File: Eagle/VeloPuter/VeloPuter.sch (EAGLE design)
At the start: 38 parts, among them IC1 LM2931, IC2 B7546, IC3 B7546

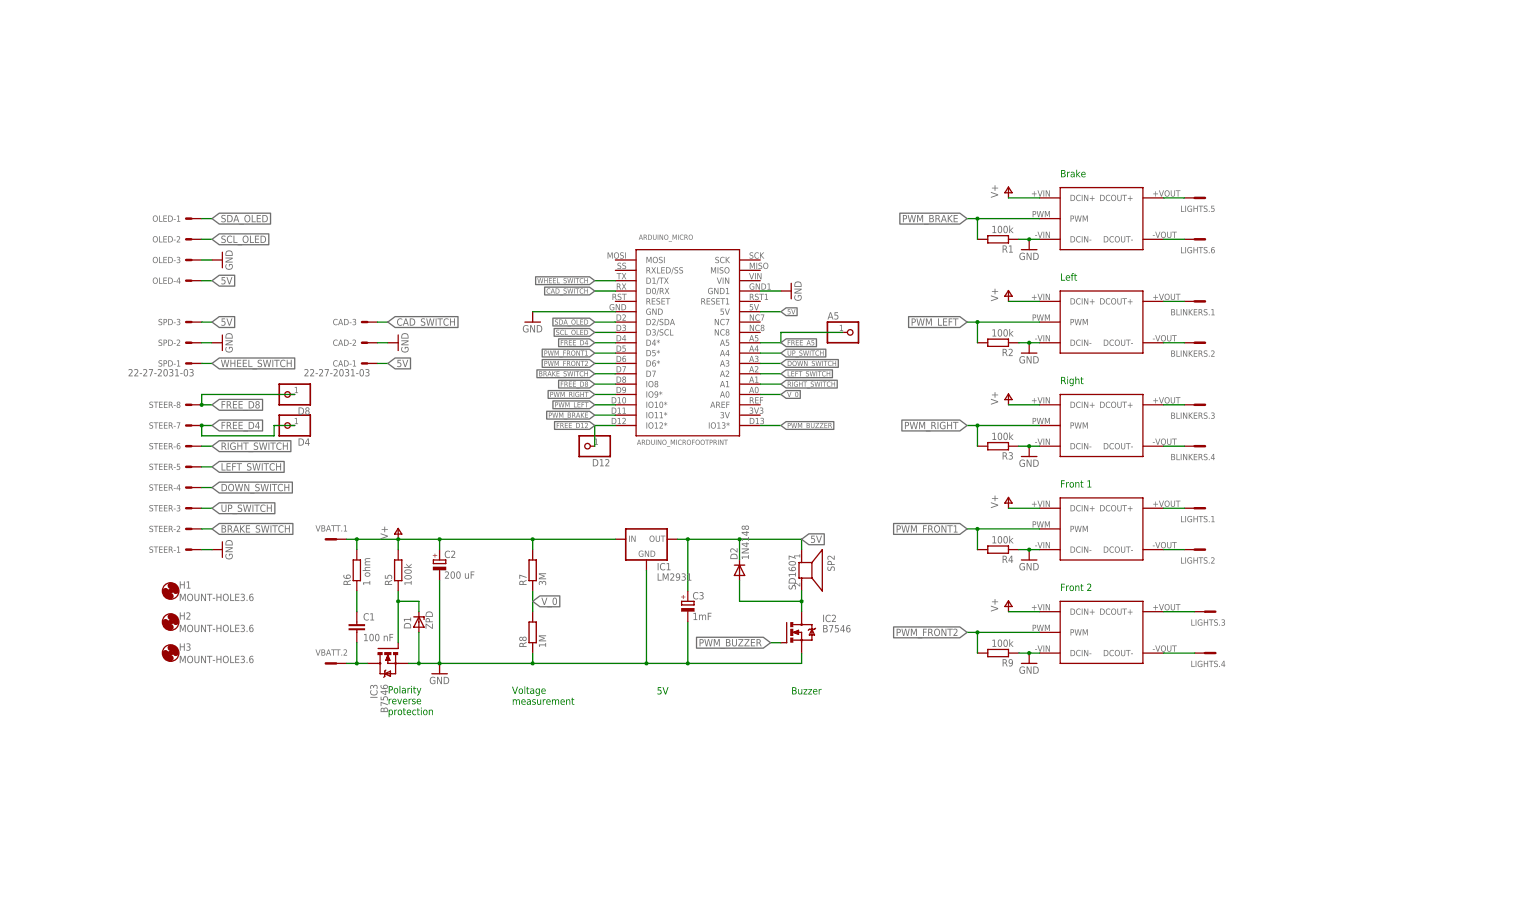
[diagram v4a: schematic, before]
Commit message: Started working on the PCB again. Adding swtichoff of the ALL Ldd's. Also: adding a 6th LDDd.
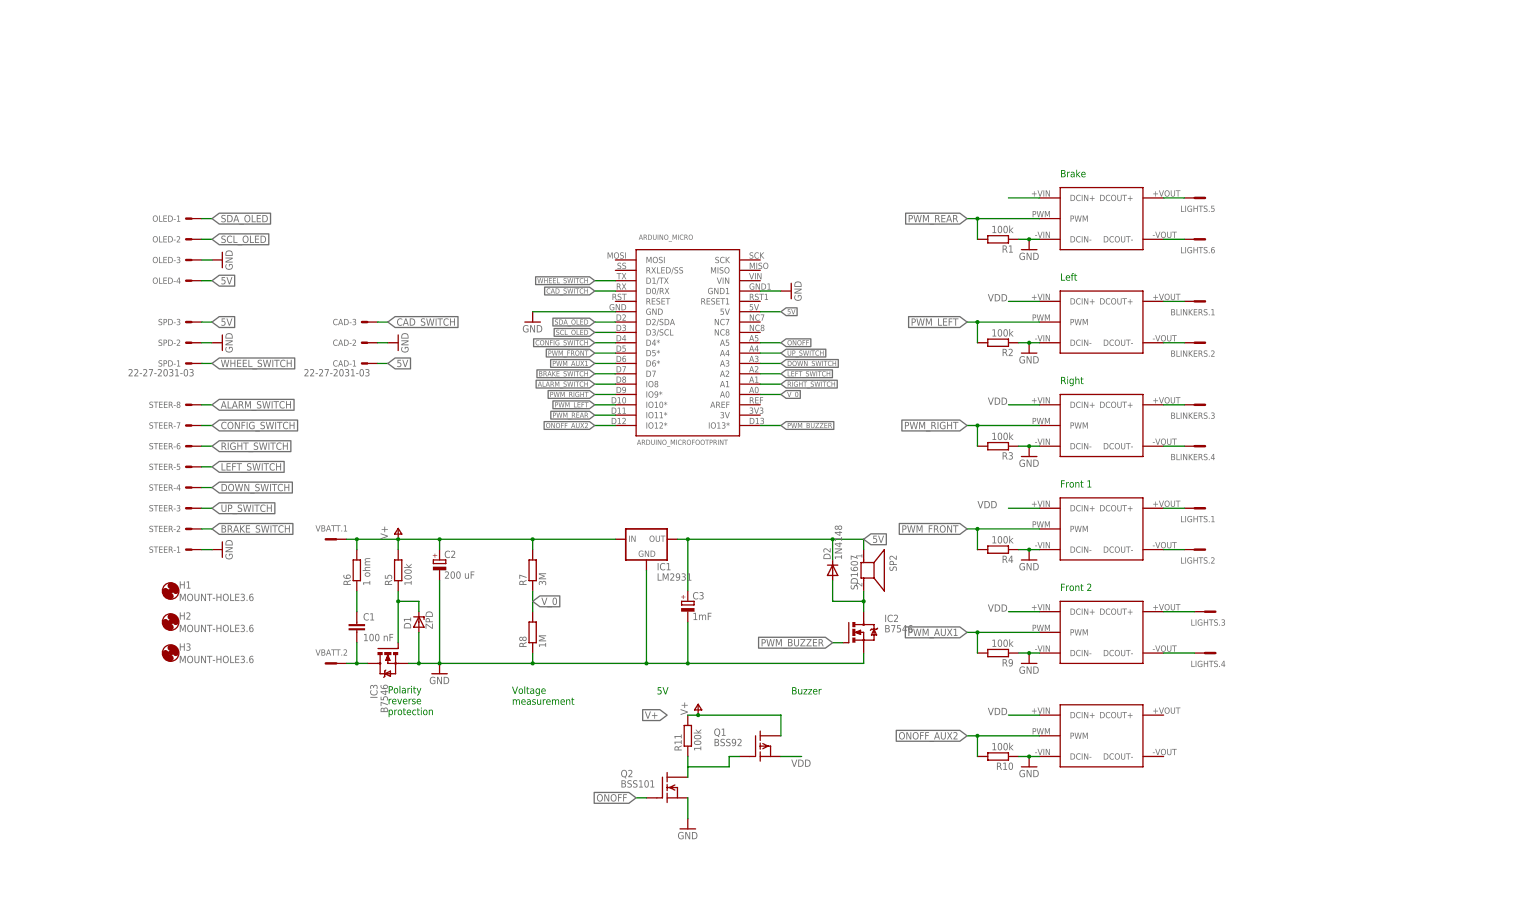
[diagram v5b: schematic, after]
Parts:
- removed A5, D12, D4, D8: (no value), pinhead:PINHD-1X1
- added Q1: BSS92, transistor-fet:BSS92
- added Q2: BSS101, transistor-fet:BSS101
- added R10, R11: 100k, resistor:R-EU_0207/10
- added U$1: LDD-L, meanwell_dcdc:LDD-L
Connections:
- net PWM_BRAKE renamed PWM_REAR
- net PWM_FRONT1 renamed PWM_FRONT
- net PWM_FRONT2 renamed PWM_AUX1
- removed net FREE_A5: A5.1, ARDUINO_MICRO.A5
- removed net FREE_D12: ARDUINO_MICRO.IO12*, D12.1
- removed net FREE_D4: ARDUINO_MICRO.D4*, D4.1, STEER-7.S
- removed net FREE_D8: ARDUINO_MICRO.IO8, D8.1, STEER-8.S
- new net ALARM_SWITCH: ARDUINO_MICRO.IO8, STEER-8.S
- new net CONFIG_SWITCH: ARDUINO_MICRO.D4*, STEER-7.S
- new net N$15: Q1.G, Q2.D, R11.1
- new net N$20: BRAKE.DCIN+
- new net ONOFF: ARDUINO_MICRO.A5, Q2.G
- new net ONOFF_AUX2: ARDUINO_MICRO.IO12*, R10.2, U$1.PWM
- new net VDD: Q1.S, U$1.DCIN+, U$2.DCIN+, U$3.DCIN+, U$4.DCIN+, U$5.DCIN+
- net GND: now also Q2.S, R10.1, U$1.DCIN-
- net V+: now also Q1.D, R11.2; no longer BRAKE.DCIN+, U$2.DCIN+, U$3.DCIN+, U$4.DCIN+, U$5.DCIN+
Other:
- moved on the sheet: D2, IC2, SP2

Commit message: - Added alternative components for the LDDs to be   placed at the same positions - Added 5V USB - Added overall Power off - Added 6th LDD/switch (was 5) -> possible also for buzzer.   Note that a key for this is NOT available. Possibly the   config or the hazzard button can be freed for this.
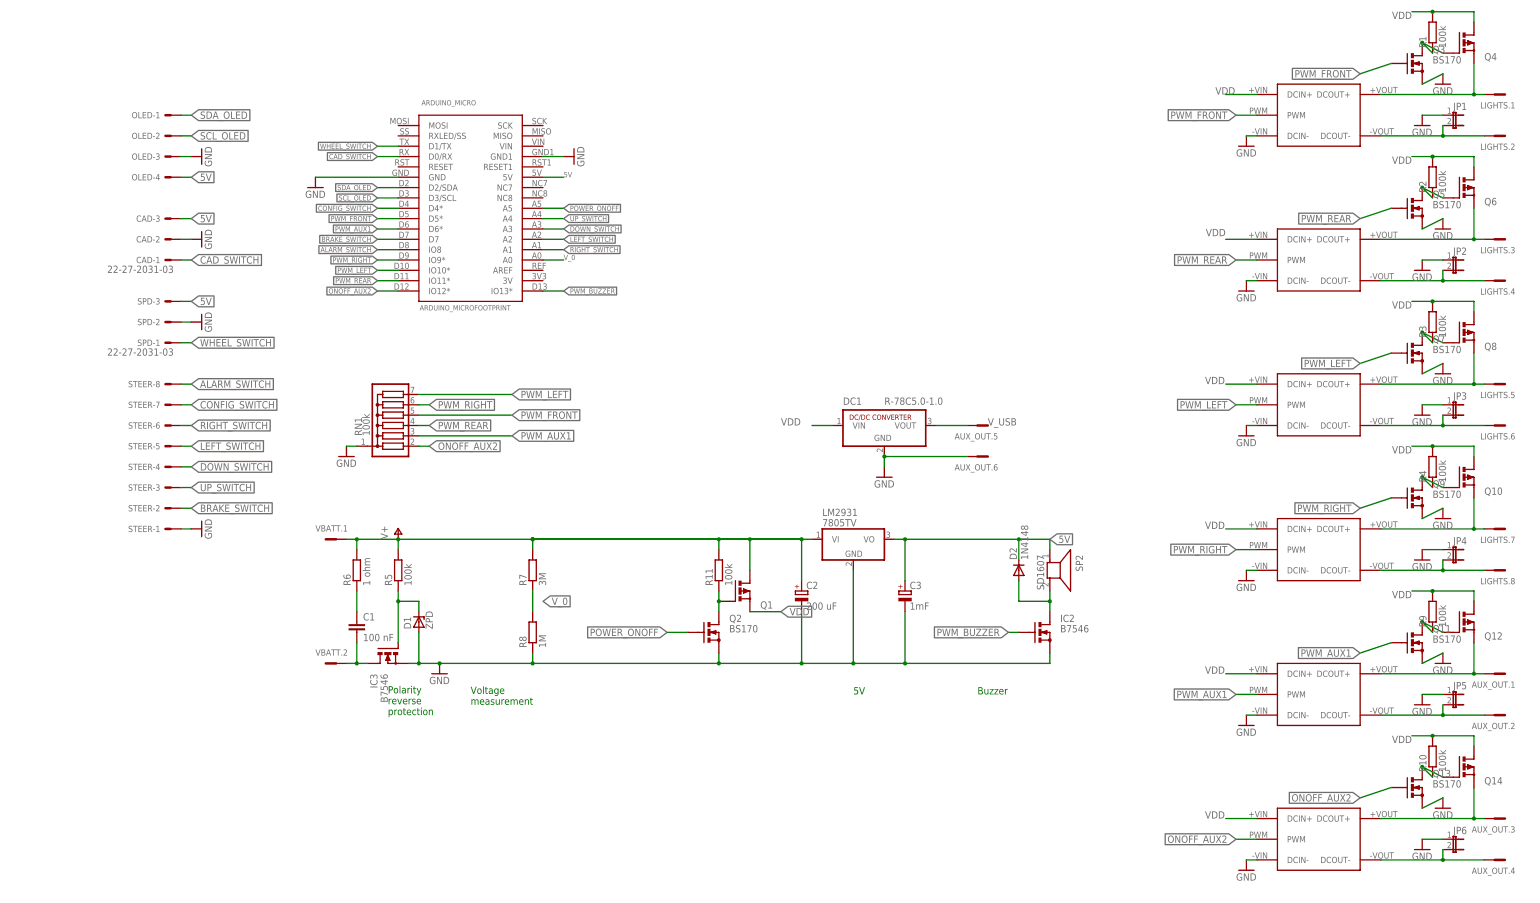
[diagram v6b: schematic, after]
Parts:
- removed BLINKERS: (no value), con-phoenix_3.81_mcv:MCV4
- removed H1, H2, H3: MOUNT-HOLE3.6, holes:MOUNT-HOLE3.6
- removed IC1: LM2931, v-reg-3-gbeu:LM2931T-L
- added AUX_OUT: Aux, con-phoenix_3.81_mcv:MCV6
- added DC1: R-78C5.0-1.0, dc-dc-converter:R-78C5.0-1.0
- added JP1, JP2, JP3, JP4, JP5, JP6: (no value), jumper:JP1E
- added LM2931: 7805TV, linear:7805TV
- added Q10, Q12, Q14, Q4, Q6, Q8: (no value), transistor-power:PMOSFET_PTO220BV
- added Q11, Q13, Q3, Q5, Q7, Q9: BS170, transistor-small-signal:BS170
- added RN1: 100k, resistor-sil:G06R
- IC2: device transistor-power:IRFZ48Z -> transistor-small-signal:BS170
- IC3: device transistor-power:IRFZ48Z -> transistor-power:PMOSFET_NTO220BV
- LIGHTS: value (none) -> Lights; device con-phoenix_3.81_mcv:MCV6 -> con-phoenix_3.81_mcv:MCV8
- Q1: value BSS92 -> (none); device transistor-fet:BSS92 -> transistor-power:PMOSFET_PTO220BV
- Q2: value BSS101 -> BS170; device transistor-fet:BSS101 -> transistor-small-signal:BS170
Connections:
- net ONOFF renamed POWER_ONOFF
- removed net N$12: LIGHTS.3.SK, U$5.DCOUT+
- new net N$17: Q3.D, Q4.G, R1.1
- new net N$23: Q7.D, Q8.G, R3.1
- new net N$28: Q10.G, Q9.D, R4.1
- new net N$29: AUX_OUT.1.SK, Q12.S, U$5.DCOUT+
- new net N$33: Q11.D, Q12.G, R9.1
- new net N$34: AUX_OUT.3.SK, Q14.S, U$1.DCOUT+
- new net N$39: AUX_OUT.4.SK, JP6.2, U$1.DCOUT-
- new net N$40: Q13.D, Q14.G, R10.1
- new net V_USB: AUX_OUT.5.SK, DC1.VOUT
- net 5V: now also CAD-3.S, LM2931.VO; no longer CAD-1.S, IC1.OUT
- net CAD_SWITCH: now also CAD-1.S; no longer CAD-3.S
- net GND: now also AUX_OUT.6.SK, DC1.GND, JP1.1, JP2.1, JP3.1, JP4.1, JP5.1, JP6.1, LM2931.GND, Q11.S, Q13.S, Q3.S, Q5.S, Q7.S, Q9.S, RN1.1; no longer IC1.GND, R1.1, R10.1, R2.1, R3.1, R4.1, R9.1
- net N$10: now also Q4.S
- net N$11: now also JP1.2
- net N$13: now also AUX_OUT.2.SK, JP5.2; no longer LIGHTS.4.SK
- net N$20: now also Q5.D, Q6.G, R2.1; no longer BRAKE.DCIN+
- net N$3: now also LIGHTS.3.SK, Q6.S; no longer LIGHTS.5.SK
- net N$5: now also JP2.2, LIGHTS.4.SK; no longer LIGHTS.6.SK
- net N$6: now also LIGHTS.5.SK, Q8.S; no longer BLINKERS.1.SK
- net N$7: now also JP3.2, LIGHTS.6.SK; no longer BLINKERS.2.SK
- net N$8: now also LIGHTS.7.SK, Q10.S; no longer BLINKERS.3.SK
- net N$9: now also JP4.2, LIGHTS.8.SK; no longer BLINKERS.4.SK
- net ONOFF_AUX2: now also Q13.G, RN1.2; no longer R10.2
- net PWM_AUX1: now also Q11.G, RN1.3; no longer R9.2
- net PWM_FRONT: now also Q3.G, RN1.5; no longer R4.2
- net PWM_LEFT: now also Q7.G, RN1.7; no longer R2.2
- net PWM_REAR: now also Q5.G, RN1.4; no longer R1.2
- net PWM_RIGHT: now also Q9.G, RN1.6; no longer R3.2
- net V+: now also LM2931.VI; no longer IC1.IN
- net VDD: now also BRAKE.DCIN+, DC1.VIN, Q10.D, Q12.D, Q14.D, Q4.D, Q6.D, Q8.D, R1.2, R10.2, R2.2, R3.2, R4.2, R9.2
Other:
- note removed: "Brake"
- note removed: "Front 1"
- note removed: "Front 2"
- note removed: "Left"
- note removed: "Right"
- moved on the sheet: ARDUINO_MICRO, C2, C3, CAD-1, CAD-2, CAD-3, D2, LIGHTS.1, LIGHTS.2, LIGHTS.3, LIGHTS.4, LIGHTS.5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

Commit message: Finished placing the components. Next: routing the connections.
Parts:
- Q1, Q10, Q12, Q14, Q4, Q6, Q8: value (none) -> 4P04L04
- R7: value 3M -> 300k
- R8: value 1M -> 100k
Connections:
- net V- renamed N$2
- net V+: no longer R7.2
- net VDD: now also R7.2
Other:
- moved on the sheet: Q1, Q2, R11, R7, R8

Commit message: Routing done. Next: tripple check everything (such as pinning, lost connections, spacings, design rules etc, etc
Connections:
- net N$10 renamed FRONT+
- net N$11 renamed FRONT-
- net N$13 renamed AUX1-
- net N$2 renamed V-
- net N$29 renamed AUX1+
- net N$3 renamed REAR+
- net N$34 renamed AUX2+
- net N$39 renamed AUX2-
- net N$5 renamed REAR-
- net N$6 renamed LEFT+
- net N$7 renamed LEFT-
- net N$8 renamed RIGHT+
- net N$9 renamed RIGHT-
- net PWM_AUX1: now also RN1.6; no longer RN1.3
- net PWM_FRONT: now also RN1.7; no longer RN1.5
- net PWM_LEFT: now also RN1.4; no longer RN1.7
- net PWM_REAR: now also RN1.3; no longer RN1.4
- net PWM_RIGHT: now also RN1.5; no longer RN1.6
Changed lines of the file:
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@@
 </segment>
 <segment>
-<label x="76.2" y="73.66" size="1.778" layer="95" xref="yes"/>
-<pinref part="RN1" gate="G$1" pin="4"/>
-<wire x1="76.2" y1="73.66" x2="73.66" y2="73.66" width="0.1524" layer="91"/>
+<label x="81.28" y="71.12" size="1.778" layer="95" xref="yes"/>
+<pinref part="RN1" gate="G$1" pin="3"/>
+<wire x1="81.28" y1="71.12" x2="73.66" y2="71.12" width="0.1524" layer="91"/>
 </segment>
 <segment>
@@
 </segment>
 </net>
-<net name="N$3" class="0">
+<net name="REAR+" class="0">
 <segment>
 <pinref part="BRAKE" gate="G$1" pin="DCOUT+"/>
@@
 </segment>
 </net>
-<net name="N$5" class="0">
+<net name="REAR-" class="0">
 <segment>
 <pinref part="BRAKE" gate="G$1" pin="DCOUT-"/>
@@
 </segment>
 </net>
-<net name="N$6" class="0">
+<net name="LEFT+" class="0">
 <segment>
 <pinref part="U$2" gate="G$1" pin="DCOUT+"/>
@@
 </segment>
 </net>
-<net name="N$7" class="0">
+<net name="LEFT-" class="0">
 <segment>
 <pinref part="U$2" gate="G$1" pin="DCOUT-"/>
@@
 </segment>
 </net>
-<net name="N$8" class="0">
+<net name="RIGHT+" class="0">
 <segment>
 <pinref part="U$3" gate="G$1" pin="DCOUT+"/>
@@
 </segment>
 </net>
-<net name="N$9" class="0">
+<net name="RIGHT-" class="0">
 <segment>
 <pinref part="U$3" gate="G$1" pin="DCOUT-"/>
@@
 </segment>
 </net>
-<net name="N$10" class="0">
+<net name="FRONT+" class="0">
 <segment>
 <pinref part="U$4" gate="G$1" pin="DCOUT+"/>
@@
 </segment>
 </net>
-<net name="N$11" class="0">
+<net name="FRONT-" class="0">
 <segment>
 <pinref part="U$4" gate="G$1" pin="DCOUT-"/>
@@
 </segment>
 </net>
-<net name="N$13" class="0">
+<net name="AUX1-" class="0">
 <segment>
 <pinref part="U$5" gate="G$1" pin="DCOUT-"/>
@@
 </segment>
 <segment>
-<label x="96.52" y="81.28" size="1.778" layer="95" xref="yes"/>
-<pinref part="RN1" gate="G$1" pin="7"/>
-<wire x1="96.52" y1="81.28" x2="73.66" y2="81.28" width="0.1524" layer="91"/>
+<label x="99.06" y="73.66" size="1.778" layer="95" xref="yes"/>
+<pinref part="RN1" gate="G$1" pin="4"/>
+<wire x1="99.06" y1="73.66" x2="73.66" y2="73.66" width="0.1524" layer="91"/>
 </segment>
 <segment>
@@
 </segment>
 <segment>
-<label x="76.2" y="78.74" size="1.778" layer="95" xref="yes"/>
-<pinref part="RN1" gate="G$1" pin="6"/>
-<wire x1="76.2" y1="78.74" x2="73.66" y2="78.74" width="0.1524" layer="91"/>
+<label x="81.28" y="76.2" size="1.778" layer="95" xref="yes"/>
+<pinref part="RN1" gate="G$1" pin="5"/>
+<wire x1="81.28" y1="76.2" x2="73.66" y2="76.2" width="0.1524" layer="91"/>
 </segment>
 <segment>
@@
 </segment>
 <segment>
-<label x="96.52" y="76.2" size="1.778" layer="95" xref="yes"/>
-<pinref part="RN1" gate="G$1" pin="5"/>
-<wire x1="96.52" y1="76.2" x2="73.66" y2="76.2" width="0.1524" layer="91"/>
+<label x="81.28" y="81.28" size="1.778" layer="95" xref="yes"/>
+<pinref part="RN1" gate="G$1" pin="7"/>
+<wire x1="81.28" y1="81.28" x2="73.66" y2="81.28" width="0.1524" layer="91"/>
 </segment>
 <segment>
@@
 </segment>
 <segment>
-<label x="96.52" y="71.12" size="1.778" layer="95" xref="yes"/>
-<pinref part="RN1" gate="G$1" pin="3"/>
-<wire x1="73.66" y1="71.12" x2="96.52" y2="71.12" width="0.1524" layer="91"/>
+<label x="99.06" y="78.74" size="1.778" layer="95" xref="yes"/>
+<pinref part="RN1" gate="G$1" pin="6"/>
+<wire x1="99.06" y1="78.74" x2="73.66" y2="78.74" width="0.1524" layer="91"/>
 </segment>
 <segment>
@@
 </segment>
 <segment>
-<label x="76.2" y="68.58" size="1.778" layer="95" xref="yes"/>
-<pinref part="RN1" gate="G$1" pin="2"/>
-<wire x1="76.2" y1="68.58" x2="73.66" y2="68.58" width="0.1524" layer="91"/>
-</segment>
-<segment>
 <pinref part="Q13" gate="1" pin="G"/>
 <wire x1="312.42" y1="-15.24" x2="304.8" y2="-17.78" width="0.1524" layer="91"/>
 <label x="304.8" y="-17.78" size="1.778" layer="95" rot="R180" xref="yes"/>
+</segment>
+<segment>
+<wire x1="73.66" y1="68.58" x2="99.06" y2="68.58" width="0.1524" layer="91"/>
+<label x="99.06" y="68.58" size="1.778" layer="95" xref="yes"/>
+<pinref part="RN1" gate="G$1" pin="2"/>
 </segment>
 </net>
@@
 </segment>
 </net>
-<net name="N$29" class="0">
+<net name="AUX1+" class="0">
 <segment>
 <pinref part="U$5" gate="G$1" pin="DCOUT+"/>
@@
 </segment>
 </net>
-<net name="N$39" class="0">
+<net name="AUX2-" class="0">
 <segment>
 <pinref part="U$1" gate="G$1" pin="DCOUT-"/>
@@
 </segment>
 </net>
-<net name="N$34" class="0">
+<net name="AUX2+" class="0">
 <segment>
 <pinref part="U$1" gate="G$1" pin="DCOUT+"/>
@@
 </segment>
 </net>
-<net name="N$2" class="0">
+<net name="V-" class="0">
 <segment>
 <pinref part="VBATT" gate=".2" pin="SK"/>
